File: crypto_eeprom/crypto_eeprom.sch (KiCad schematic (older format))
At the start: 3 parts, among them J1 EXPANSION_BOTTOM, U1 ATSHA204A

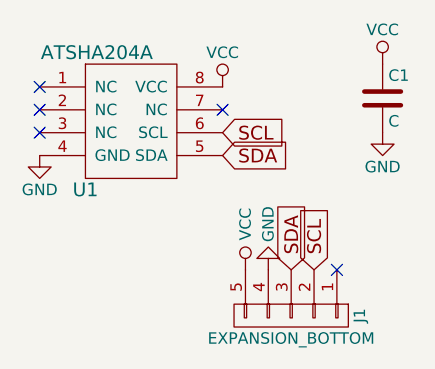
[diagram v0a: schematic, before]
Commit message: Redesigned to use new footprint and UDFN IC
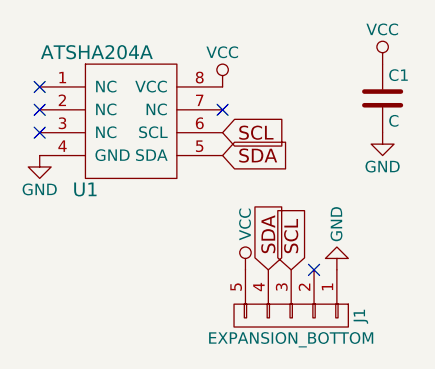
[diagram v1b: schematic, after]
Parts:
- C1: footprint Capacitors_SMD:C_0603_HandSoldering -> Capacitors_SMD:C_0603
- U1: footprint Housings_SOIC:SOIC-8_3.9x4.9mm_Pitch1.27mm -> footprints:DFN-8_3x2mm_Pitch0.5mm
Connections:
- net GND: now also J1.1 (P1); no longer J1.4 (P4)
- net SCL: now also J1.3 (P3); no longer J1.2 (P2)
- net SDA: now also J1.4 (P4); no longer J1.3 (P3)
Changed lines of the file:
@@
 LIBS:valves
 LIBS:atsha204a
+LIBS:crypto_eeprom-cache
 EELAYER 25 0
 EELAYER END
@@
 F 0 "U1" H 5300 3550 60  0000 C CNN
 F 1 "ATSHA204A" H 5350 4150 60  0000 C CNN
-F 2 "Housings_SOIC:SOIC-8_3.9x4.9mm_Pitch1.27mm" H 5500 3850 60  0001 C CNN
+F 2 "footprints:DFN-8_3x2mm_Pitch0.5mm" H 5500 3850 60  0001 C CNN
 F 3 "" H 5500 3850 60  0001 C CNN
 	1    5500 3850
@@
 F 0 "C1" H 6625 3850 50  0000 L CNN
 F 1 "C" H 6625 3650 50  0000 L CNN
-F 2 "Capacitors_SMD:C_0603_HandSoldering" H 6638 3600 50  0001 C CNN
+F 2 "Capacitors_SMD:C_0603" H 6638 3600 50  0001 C CNN
 F 3 "" H 6600 3750 50  0001 C CNN
 	1    6600 3750
@@
 L GND #PWR05
 U 1 1 5960AD91
-P 6100 4500
-F 0 "#PWR05" H 6100 4250 50  0001 C CNN
-F 1 "GND" V 6100 4300 50  0000 C CNN
-F 2 "" H 6100 4500 50  0001 C CNN
-F 3 "" H 6100 4500 50  0001 C CNN
-	1    6100 4500
+P 6400 4500
+F 0 "#PWR05" H 6400 4250 50  0001 C CNN
+F 1 "GND" V 6400 4300 50  0000 C CNN
+F 2 "" H 6400 4500 50  0001 C CNN
+F 3 "" H 6400 4500 50  0001 C CNN
+	1    6400 4500
 	-1   0    0    1
 $EndComp
@@
 	1    0    0    -1
 $EndComp
-Text GLabel 6300 4500 1    60   Input ~ 0
+Text GLabel 6200 4500 1    60   Input ~ 0
 SCL
-Text GLabel 6200 4500 1    60   Input ~ 0
+Text GLabel 6100 4500 1    60   Input ~ 0
 SDA
-NoConn ~ 6400 4500
+NoConn ~ 6300 4500
 $EndSCHEMATC
